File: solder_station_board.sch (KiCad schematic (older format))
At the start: 43 parts, among them J1 PWR_5_V, J2 INPUT, J3 RT_WELLER, J4 INPUT, J5 VFD_DISPLAY, J6 PWR_15V, J8 SERIAL, P1 ISP, Q1 IRF9540, Q2 2N7002, U4 TLC272, U5 LT1007, U6 ATMEGA168-20AU

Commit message: jbc
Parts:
- removed C1, C13, C7: 10n, Capacitor_SMD:C_0805_2012Metric_Pad1.15x1.40mm_HandSolder, symbol Device:C_Small
- removed D1: BAT54S, Package_TO_SOT_SMD:SOT-23, symbol Diode:BAT54S
- removed D8: 4V7, Diode_SMD:D_MicroMELF_Hadsoldering, symbol Device:D_Zener
- removed J1: PWR_5_V, Connector_PinSocket_2.54mm:PinSocket_1x03_P2.54mm_Vertical, symbol Connector_Generic:Conn_01x03
- removed J2, J4: INPUT, Connector_PinHeader_2.54mm:PinHeader_1x04_P2.54mm_Vertical, symbol Connector_Generic:Conn_01x04
- removed J3: RT_WELLER, Connector_PinSocket_2.54mm:PinSocket_1x03_P2.54mm_Vertical, symbol Connector_Generic:Conn_01x03
- removed J5: VFD_DISPLAY, Connector_PinHeader_2.54mm:PinHeader_1x05_P2.54mm_Vertical, symbol Connector_Generic:Conn_01x05
- removed Q1: IRF9540, Package_TO_SOT_THT:TO-220-3_Horizontal_TabDown, symbol Device:Q_PMOS_GDS
- removed Q2: 2N7002, Package_TO_SOT_SMD:SOT-23, symbol Transistor_FET:2N7002
- removed R1, R2: 0, Resistor_SMD:R_1206_3216Metric, symbol Device:R_Small
- removed R10, R11, R13, R16, R4, R9: 1k, Resistor_SMD:R_0805_2012Metric_Pad1.15x1.40mm_HandSolder, symbol Device:R_Small
- removed R12: 22k, Resistor_SMD:R_0805_2012Metric_Pad1.15x1.40mm_HandSolder, symbol Device:R_Small
- removed R14: 33k, Resistor_SMD:R_0805_2012Metric_Pad1.15x1.40mm_HandSolder, symbol Device:R_Small
- removed R15: 10K, Resistor_SMD:R_0805_2012Metric_Pad1.15x1.40mm_HandSolder, symbol Device:R_Small
- removed R5: 5k6, Resistor_SMD:R_0805_2012Metric_Pad1.15x1.40mm_HandSolder, symbol Device:R_Small
- removed R6: 4k7, Resistor_SMD:R_0805_2012Metric_Pad1.15x1.40mm_HandSolder, symbol Device:R_Small
- removed R7: 100k, Resistor_SMD:R_0805_2012Metric_Pad1.15x1.40mm_HandSolder, symbol Device:R_Small
- removed R8: 2k2, Resistor_SMD:R_0805_2012Metric_Pad1.15x1.40mm_HandSolder, symbol Device:R_Small
- removed TP1, TP2, TP3: tp, Connector_Wire:SolderWirePad_1x01_Drill0.8mm, symbol solder_station_board-rescue:TestPoint-Connector
- removed U4: TLC272, Package_SO:SOIC-8_3.9x4.9mm_P1.27mm, symbol Amplifier_Operational:TLC272
- removed U5: LT1007, Package_SO:SOIC-8_3.9x4.9mm_P1.27mm, symbol Amplifier_Operational:LT1012
- added C1: 100u, Capacitor_THT:CP_Radial_D8.0mm_P3.50mm, symbol solder_station_board-rescue:CP-Device
- added C10, C3, C5, C6, C7: 100n, Capacitor_SMD:C_0805_2012Metric_Pad1.15x1.40mm_HandSolder, symbol solder_station_board-rescue:C-Device
- added C11, C12: 10n, Capacitor_SMD:C_0603_1608Metric_Pad1.05x0.95mm_HandSolder, symbol Device:C_Small
- added C4: 10u, Capacitor_SMD:C_2512_6332Metric_Pad1.52x3.35mm_HandSolder, symbol solder_station_board-rescue:CP-Device
- added D1, D2: BAT54S, Package_TO_SOT_SMD:SOT-23, symbol solder_station_board-rescue:BAT54S-Diode
- added D3: LED, LED_SMD:LED_0603_1608Metric_Castellated, symbol Device:LED
- added D5: GBU4A, custom:Diode_Bridge_Vishay_GBU_20P3.8mm, symbol solder_station_board-rescue:GBU4A-Diode_Bridge
- added FB1, FB2, FB3, FB4, FB5, FB6: ferrite, Inductor_SMD:L_0805_2012Metric_Pad1.15x1.40mm_HandSolder, symbol Device:Ferrite_Bead_Small
- added J1: LCD 5110, Connector_PinSocket_2.54mm:PinSocket_1x08_P2.54mm_Vertical, symbol Connector_Generic:Conn_01x08
- added J2: SENSE, Connector_PinHeader_2.54mm:PinHeader_1x05_P2.54mm_Vertical, symbol solder_station_board-rescue:Conn_01x05-Connector_Generic
- added J7: ROTARY, Connector_PinHeader_2.54mm:PinHeader_1x05_P2.54mm_Vertical, symbol solder_station_board-rescue:Conn_01x05-Connector_Generic
- added R1, R18: 330, Resistor_SMD:R_0603_1608Metric_Pad1.05x0.95mm_HandSolder, symbol solder_station_board-rescue:R-Device
- added R19, R2, R20, R21, R22, R23: 1k, Resistor_SMD:R_0603_1608Metric_Pad1.05x0.95mm_HandSolder, symbol solder_station_board-rescue:R-Device
- added U2: PC817, Package_DIP:DIP-4_W7.62mm, symbol solder_station_board-rescue:PC817-Isolator
- added U3: LT1117-3.3, Package_TO_SOT_SMD:SOT-223-3_TabPin2, symbol solder_station_board-rescue:LT1117-3.3-Regulator_Linear
- added U4, U5, U7: MAX31855KASA, Package_SO:SOIC-8_3.9x4.9mm_P1.27mm, symbol Sensor_Temperature:MAX31855KASA
- C2: footprint Capacitor_SMD:C_0805_2012Metric_Pad1.15x1.40mm_HandSolder -> Capacitor_SMD:C_0603_1608Metric_Pad1.05x0.95mm_HandSolder
- C8, C9: symbol Device:C_Small -> solder_station_board-rescue:C_Small-Device
- J6: value PWR_15V -> PWR_5AV; footprint Connector_Wire:SolderWirePad_1x02_P5.08mm_Drill1.5mm -> TerminalBlock_MetzConnect:TerminalBlock_MetzConnect_Type101_RT01602HBWC_1x02_P5.08mm_Horizontal; symbol Connector_Generic:Conn_01x02 -> solder_station_board-rescue:Conn_01x02-Connector_Generic
- J8: symbol Connector_Generic:Conn_01x03 -> solder_station_board-rescue:Conn_01x03-Connector_Generic
- MH1, MH2, MH3, MH4: symbol Mechanical:MountingHole_Pad -> solder_station_board-rescue:MountingHole_Pad-Mechanical
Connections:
- net labels added: +3.3V, ASENSE0, ASENSE1, DIS_CLK, DIS_DIN, DIS_D\C, DIS_LED, DIS_RST, DIS_SCE, GNDA, MAX_CS0, MAX_CS1, MAX_CS2, MAX_SCK, MAX_SO, RED0, RED1, RED2, SENSE0, SENSE1, SOLDER0, SOLDER1, SOLDER2, TACK
- net labels removed: +15V, +5V, -5V, INP1, INP2, INP3, INP4, INP5, INP6, SOLDER, TEMP, VFD_DATA, VFD_RCLK, VFD_SRCLK, ~VFD_SRCLR
- wire segments 160 -> 193
- no-connect marks 15 -> 5
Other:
- moved on the sheet: C8, C9, P1, U6

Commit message: analog done
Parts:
- removed C1: 100u, Capacitor_THT:CP_Radial_D8.0mm_P3.50mm, symbol solder_station_board-rescue:CP-Device
- removed C11, C12: 10n, Capacitor_SMD:C_0603_1608Metric_Pad1.05x0.95mm_HandSolder, symbol Device:C_Small
- removed C3, C5, C6, C7: 100n, Capacitor_SMD:C_0805_2012Metric_Pad1.15x1.40mm_HandSolder, symbol solder_station_board-rescue:C-Device
- removed C4: 10u, Capacitor_SMD:C_2512_6332Metric_Pad1.52x3.35mm_HandSolder, symbol solder_station_board-rescue:CP-Device
- removed D1, D2: BAT54S, Package_TO_SOT_SMD:SOT-23, symbol solder_station_board-rescue:BAT54S-Diode
- removed D5: GBU4A, custom:Diode_Bridge_Vishay_GBU_20P3.8mm, symbol solder_station_board-rescue:GBU4A-Diode_Bridge
- removed FB3, FB4, FB5, FB6: ferrite, Inductor_SMD:L_0805_2012Metric_Pad1.15x1.40mm_HandSolder, symbol Device:Ferrite_Bead_Small
- removed J6: PWR_5AV, TerminalBlock_MetzConnect:TerminalBlock_MetzConnect_Type101_RT01602HBWC_1x02_P5.08mm_Horizontal, symbol solder_station_board-rescue:Conn_01x02-Connector_Generic
- removed R1: 330, Resistor_SMD:R_0603_1608Metric_Pad1.05x0.95mm_HandSolder, symbol solder_station_board-rescue:R-Device
- removed R22, R23: 1k, Resistor_SMD:R_0603_1608Metric_Pad1.05x0.95mm_HandSolder, symbol solder_station_board-rescue:R-Device
- removed U2: PC817, Package_DIP:DIP-4_W7.62mm, symbol solder_station_board-rescue:PC817-Isolator
- removed U3: LT1117-3.3, Package_TO_SOT_SMD:SOT-223-3_TabPin2, symbol solder_station_board-rescue:LT1117-3.3-Regulator_Linear
- removed U5, U7: MAX31855KASA, Package_SO:SOIC-8_3.9x4.9mm_P1.27mm, symbol Sensor_Temperature:MAX31855KASA
- U4: symbol Sensor_Temperature:MAX31855KASA -> solder_station_board-rescue:MAX31855KASA-Sensor_Temperature
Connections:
- net labels added: HEAT0, TACHO
- net labels removed: MAX_CS1, MAX_CS2, RED1, RED2, SOLDER0, TACK
- wire segments 193 -> 104
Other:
- moved on the sheet: C8, C9, D3, J7, J8, R18, U6

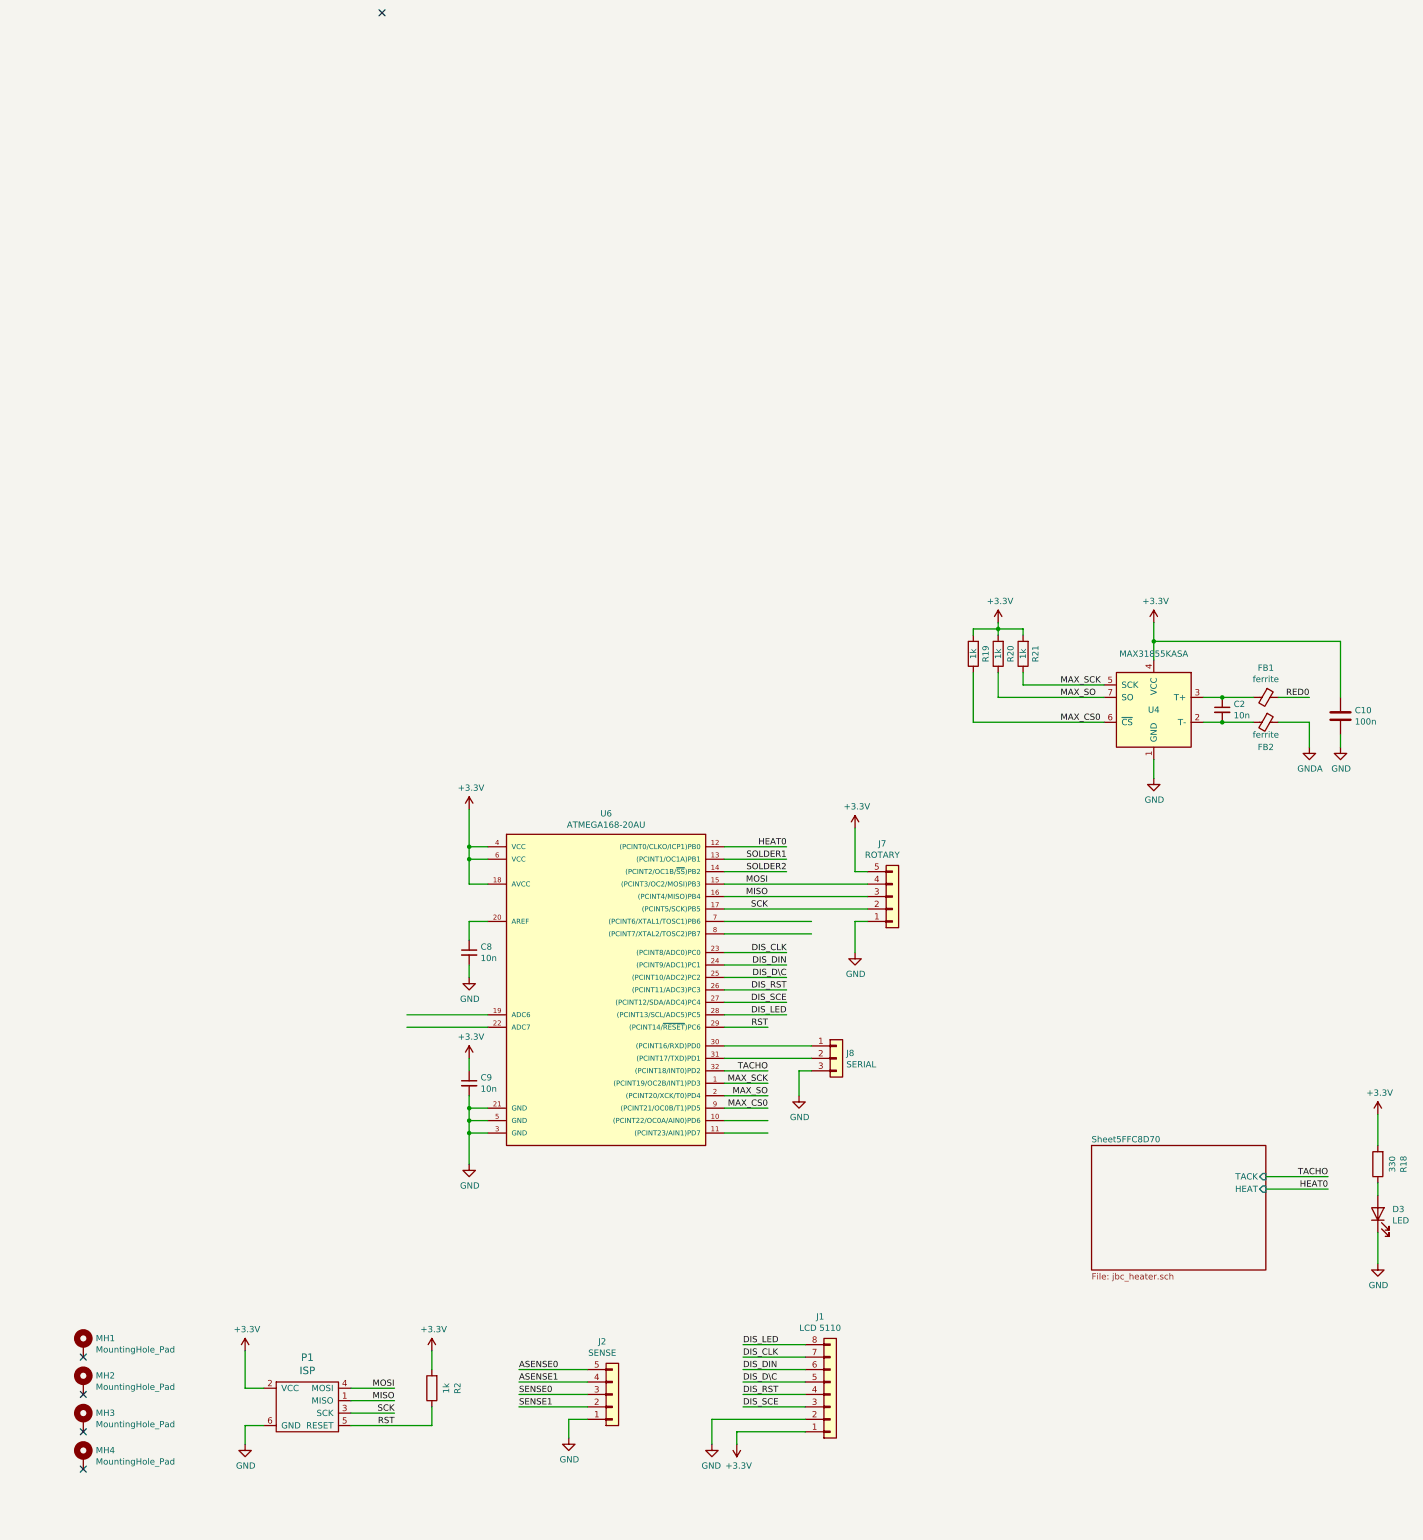
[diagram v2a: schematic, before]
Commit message: remover extra sheet
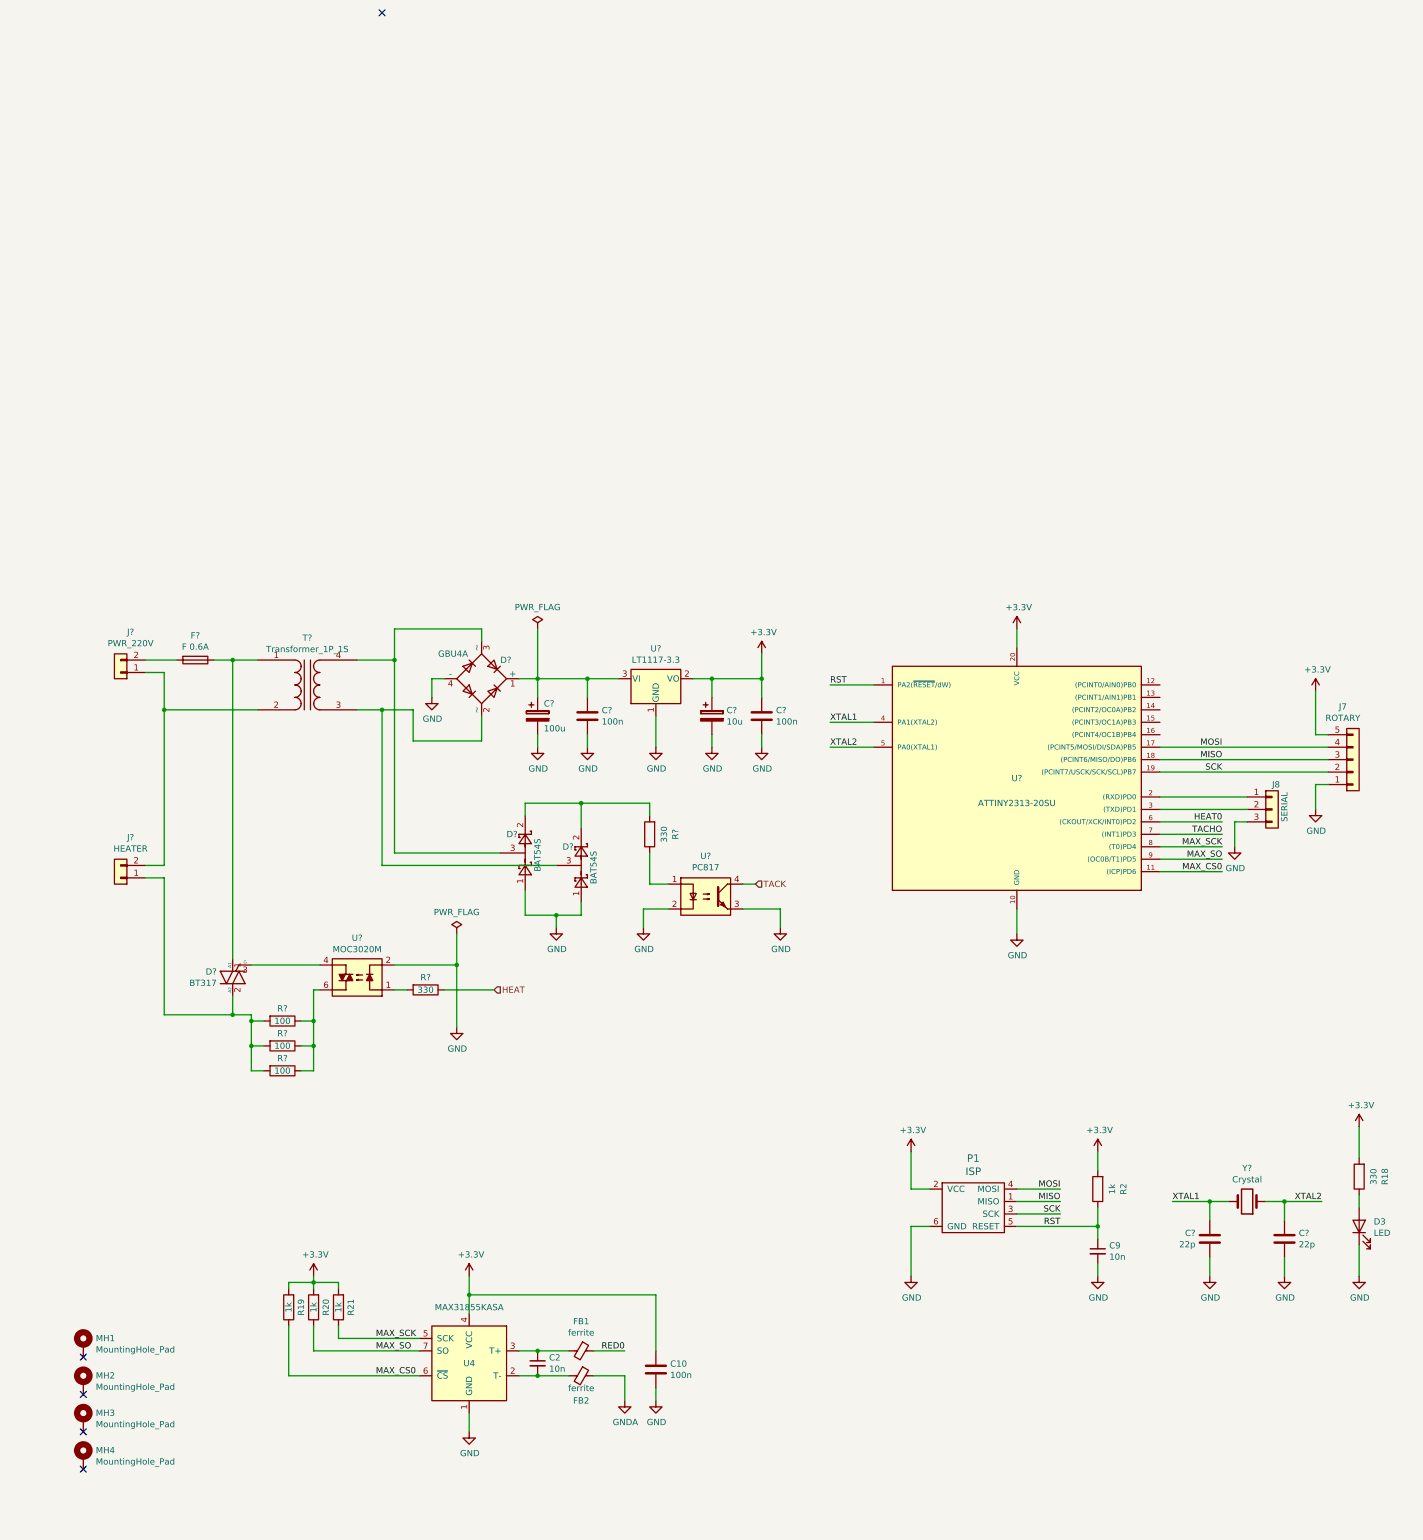
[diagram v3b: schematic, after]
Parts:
- removed C8: 10n, Capacitor_SMD:C_0805_2012Metric_Pad1.15x1.40mm_HandSolder, symbol solder_station_board-rescue:C_Small-Device
- removed J1: LCD 5110, Connector_PinSocket_2.54mm:PinSocket_1x08_P2.54mm_Vertical, symbol Connector_Generic:Conn_01x08
- removed J2: SENSE, Connector_PinHeader_2.54mm:PinHeader_1x05_P2.54mm_Vertical, symbol solder_station_board-rescue:Conn_01x05-Connector_Generic
- removed U6: ATMEGA168-20AU, Package_QFP:TQFP-32_7x7mm_P0.8mm, symbol solder_station_board-rescue:ATMEGA168-20AU-atmel
- added C? (x2): 22p, symbol Device:C
- added C? (x2): 100n, Capacitor_SMD:C_0805_2012Metric_Pad1.15x1.40mm_HandSolder, symbol solder_station_board-rescue:C-Device
- added C?: 10u, Capacitor_SMD:C_2512_6332Metric_Pad1.52x3.35mm_HandSolder, symbol solder_station_board-rescue:CP-Device
- added C?: 100u, Capacitor_THT:CP_Radial_D8.0mm_P3.50mm, symbol solder_station_board-rescue:CP-Device
- added D?: GBU4A, custom:Diode_Bridge_Vishay_GBU_20P3.8mm, symbol solder_station_board-rescue:GBU4A-Diode_Bridge
- added D? (x2): BAT54S, Package_TO_SOT_SMD:SOT-23, symbol solder_station_board-rescue:BAT54S-Diode
- added D?: BT317, symbol Device:Q_TRIAC_A1A2G
- added F?: F 0.6A, symbol Device:Fuse
- added J?: PWR_220V, TerminalBlock_MetzConnect:TerminalBlock_MetzConnect_Type101_RT01602HBWC_1x02_P5.08mm_Horizontal, symbol solder_station_board-rescue:Conn_01x02-Connector_Generic
- added J?: HEATER, TerminalBlock_MetzConnect:TerminalBlock_MetzConnect_Type101_RT01602HBWC_1x02_P5.08mm_Horizontal, symbol solder_station_board-rescue:Conn_01x02-Connector_Generic
- added R?: 330, Resistor_SMD:R_0603_1608Metric_Pad1.05x0.95mm_HandSolder, symbol solder_station_board-rescue:R-Device
- added R? (x3): 100, symbol Device:R
- added R?: 330, symbol Device:R
- added T?: Transformer_1P_1S, symbol Device:Transformer_1P_1S
- added U?: ATTINY2313-20SU, Housings_SOIC:SOIC-20W_7.5x12.8mm_Pitch1.27mm, symbol atmel:ATTINY2313-20SU
- added U?: LT1117-3.3, Package_TO_SOT_SMD:SOT-223-3_TabPin2, symbol solder_station_board-rescue:LT1117-3.3-Regulator_Linear
- added U?: PC817, Package_DIP:DIP-4_W7.62mm, symbol solder_station_board-rescue:PC817-Isolator
- added U?: MOC3020M, symbol Relay_SolidState:MOC3020M
- added Y?: Crystal, symbol Device:Crystal
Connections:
- net labels added: HEAT, TACK, XTAL1, XTAL2
- net labels removed: ASENSE0, ASENSE1, DIS_CLK, DIS_DIN, DIS_D\C, DIS_LED, DIS_RST, DIS_SCE, SENSE0, SENSE1, SOLDER1, SOLDER2
- wire segments 104 -> 150
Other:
- moved on the sheet: C10, C2, C9, D3, FB1, FB2, J7, J8, P1, R18, R19, R2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

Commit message: place
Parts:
- removed C10: 100n, Capacitor_SMD:C_0805_2012Metric_Pad1.15x1.40mm_HandSolder, symbol solder_station_board-rescue:C-Device
- removed C2: 10n, Capacitor_SMD:C_0603_1608Metric_Pad1.05x0.95mm_HandSolder, symbol Device:C_Small
- removed C? (x2): 22p, symbol Device:C
- removed FB1, FB2: ferrite, Inductor_SMD:L_0805_2012Metric_Pad1.15x1.40mm_HandSolder, symbol Device:Ferrite_Bead_Small
- removed R19, R20, R21: 1k, Resistor_SMD:R_0603_1608Metric_Pad1.05x0.95mm_HandSolder, symbol solder_station_board-rescue:R-Device
- removed T?: Transformer_1P_1S, symbol Device:Transformer_1P_1S
- removed U4: MAX31855KASA, Package_SO:SOIC-8_3.9x4.9mm_P1.27mm, symbol solder_station_board-rescue:MAX31855KASA-Sensor_Temperature
- removed Y?: Crystal, symbol Device:Crystal
- added J3: IO, Connector_JST:JST_XH_B6B-XH-A_1x06_P2.50mm_Vertical, symbol Connector_Generic:Conn_01x06
- added J4: TEMP, Connector_JST:JST_XH_B5B-XH-A_1x05_P2.50mm_Vertical, symbol solder_station_board-rescue:Conn_01x05-Connector_Generic
- added T1: Transformer_1P_2S, custom:TRAFO_1P_2S, symbol Device:Transformer_1P_2S
- D1: renamed from D?; footprint (none) -> Package_TO_SOT_THT:TO-126-3_Vertical
- D3: footprint LED_SMD:LED_0603_1608Metric_Castellated -> LED_THT:LED_D3.0mm
- F1: renamed from F?; footprint (none) -> custom:Fuseholder_Cylinder-5x20mmP1.5_Schurter_0031_8201_Horizontal_Open
- R1, R3, R4: renamed from R?; footprint (none) -> Resistor_SMD:R_1206_3216Metric
- R5: renamed from R?; footprint (none) -> Resistor_SMD:R_0603_1608Metric_Pad1.05x0.95mm_HandSolder
- U1: renamed from U?; footprint (none) -> Package_DIP:DIP-6_W7.62mm_LongPads
- U5: renamed from U?; footprint Housings_SOIC:SOIC-20W_7.5x12.8mm_Pitch1.27mm -> Package_SO:SOIC-20W_7.5x12.8mm_P1.27mm
- gave numbers to parts that had none: 12
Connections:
- net HEAT0 is gone; now on net HEAT: U5.6 ((CKOUT/XCK/INT0)PD2)
- net TACHO is gone; now on net TACK: U5.7 ((INT1)PD3)
- net +3V3: now also J4.5 (Pin_5)
- net GND: now also J8.1 (Pin_1), J3.1 (Pin_1), J4.1 (Pin_1); no longer J8.3 (Pin_3)
- net MAX_CS0: now also J4.2 (Pin_2)
- net MAX_SCK: now also J4.4 (Pin_4)
- net MAX_SO: now also J4.3 (Pin_3)
- net MISO: now also J3.3 (Pin_3); no longer J7.3 (Pin_3)
- net MOSI: now also J3.4 (Pin_4); no longer J7.4 (Pin_4)
- net at U5.2 ((RXD)PD0): now also J8.3 (Pin_3); no longer J8.1 (Pin_1)
- net ROTA: now reaches U5.12 ((PCINT0/AIN0)PB0)
- net ROTA: now also J7.4 (Pin_4)
- net ROTB: now reaches U5.13 ((PCINT1/AIN1)PB1)
- net ROTB: now also J7.3 (Pin_3)
- net ROTC: now reaches U5.14 ((PCINT2/OC0A)PB2)
- net ROTC: now also J7.2 (Pin_2)
- net PB3: now reaches U5.15 ((PCINT3/OC1A)PB3)
- net PB3: now also J3.6 (Pin_6)
- net PB4: now reaches U5.16 ((PCINT4/OC1B)PB4)
- net PB4: now also J3.5 (Pin_5)
- net at J1.1 (Pin_1), J2.2 (Pin_2): now also T1.2 (AB)
- net at D2.2 (~~), D5.3: now also T1.6 (SD)
- net at D2.3 (~~), D4.3: now also T1.3 (SA)
- net at D1.1 (A1), F1.1: now also T1.1 (AA)
- net SCK renamed PB7
- net PB7: now also J3.2 (Pin_2); no longer J7.2 (Pin_2)
- new net: T1.4 (SB), T1.5 (SC)
- no-connect marks 5 -> 7
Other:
- moved on the sheet: C9, F1, J1, J7, P1, R2
